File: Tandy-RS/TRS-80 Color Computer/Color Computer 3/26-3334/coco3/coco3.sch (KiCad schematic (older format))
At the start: 5 parts, among them CN1 Conn_02x20_Odd_Even

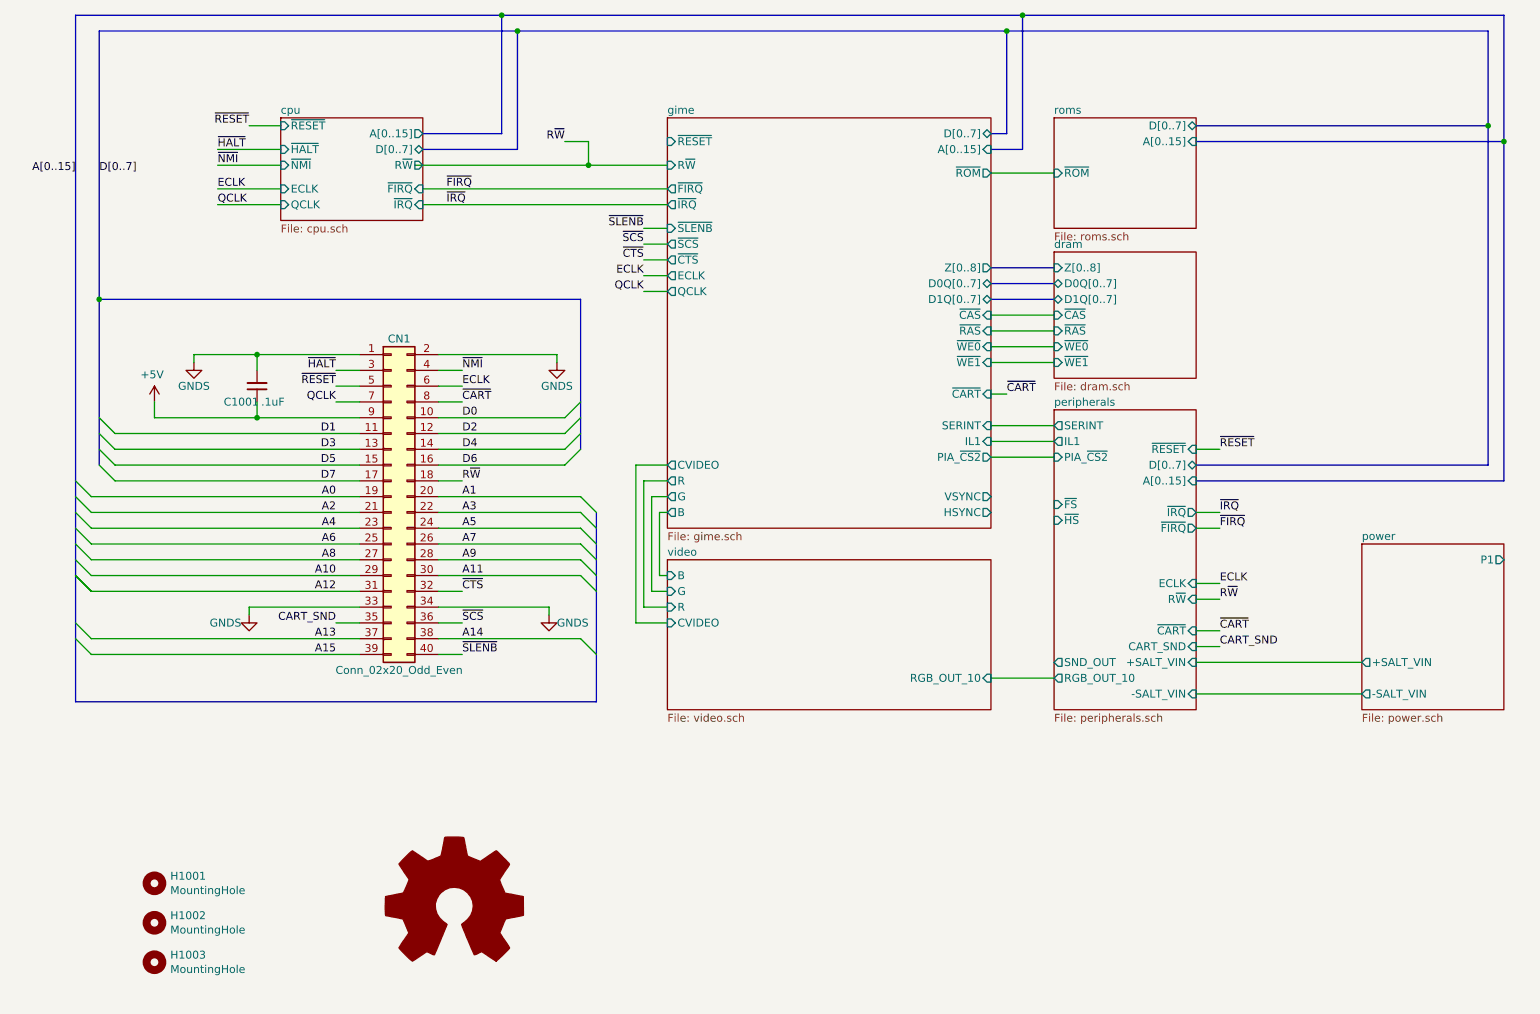
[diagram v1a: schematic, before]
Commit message: cleaned up the peripherals sheet a little
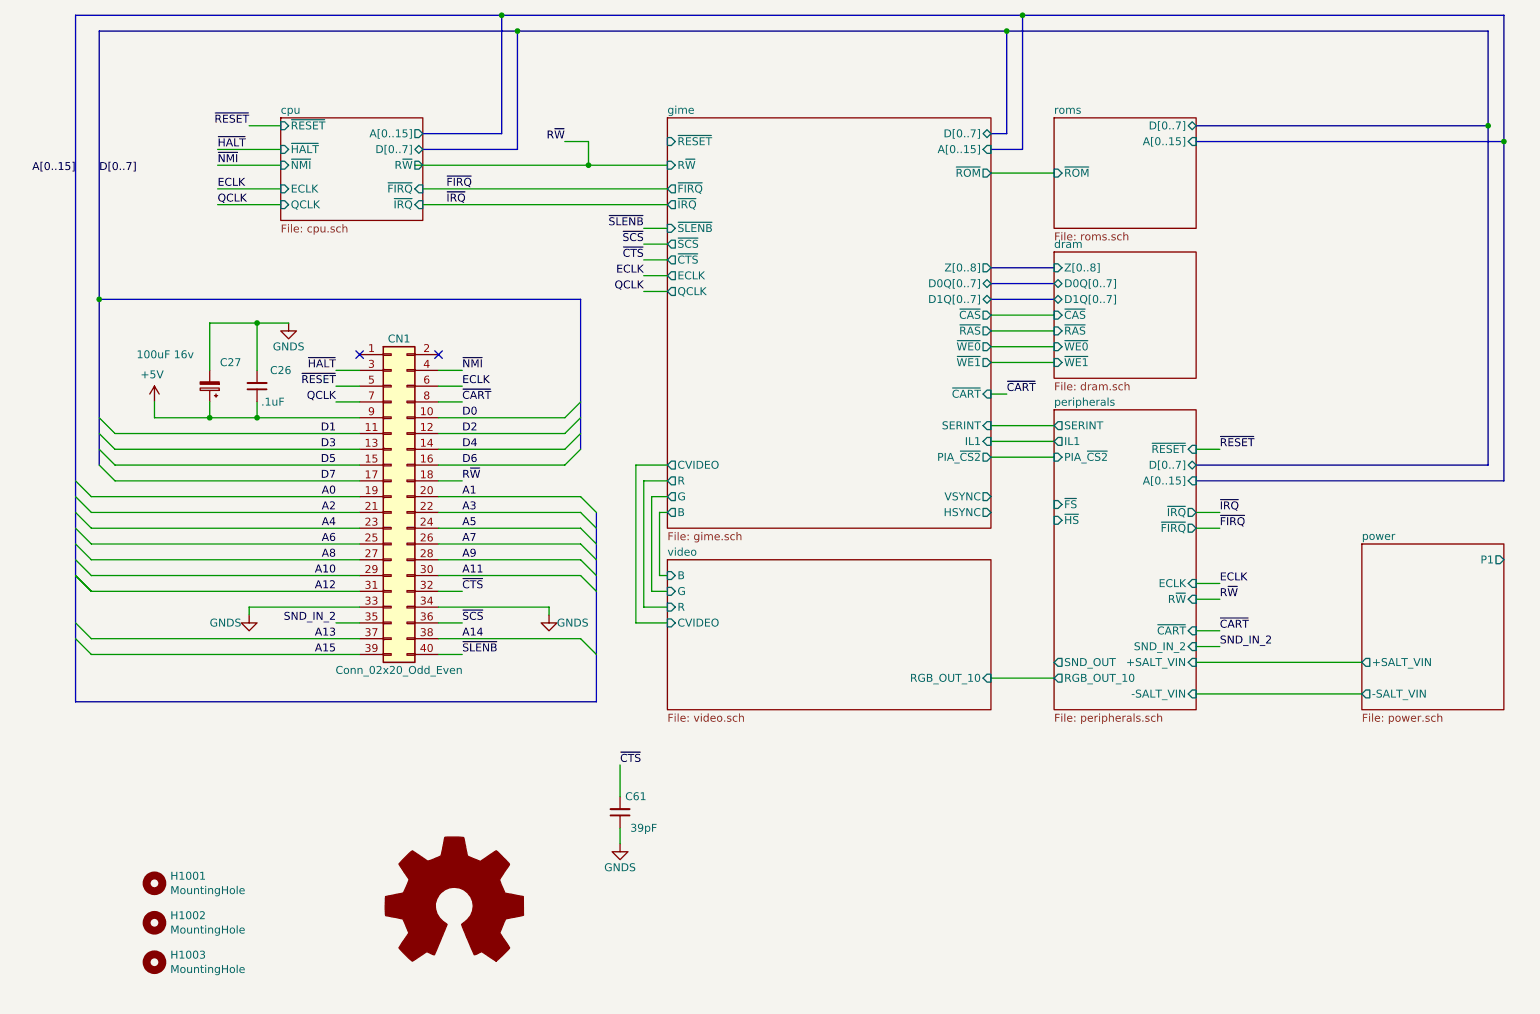
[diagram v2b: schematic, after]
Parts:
- added C27: 100uF 16v, Capacitor_THT:CP_Radial_D8.0mm_P5.00mm, symbol Device:CP_Small
- added C61: 39pF, Capacitor_THT:C_Disc_D4.7mm_W2.5mm_P5.00mm, symbol Device:C_Small
- renumbered C1001 to C26
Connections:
- net +5V: now also C27.1
- net GNDS: now also C27.2, C61.1; no longer CN1.1 (Pin_1), CN1.2 (Pin_2)
- net ~CTS: now also C61.2
- net CART_SND renamed SND_IN_2
- no-connect marks 0 -> 2
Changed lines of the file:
@@
 	8100 5350 7950 5350
 Text Label 8100 5450 0    50   ~ 0
-CART_SND
+SND_IN_2
 Wire Wire Line
 	8100 5450 7950 5450
@@
 D[0..7]
 Wire Wire Line
-	2000 3600 2650 3600
-Wire Wire Line
 	2000 4000 2650 4000
 Connection ~ 2000 4000
 Wire Wire Line
 	2000 3900 2000 4000
-Connection ~ 2000 3600
-Wire Wire Line
-	2000 3700 2000 3600
-Wire Wire Line
-	1600 3600 2000 3600
-Wire Wire Line
-	1350 4000 2000 4000
+Wire Wire Line
+	1350 4000 1700 4000
 Wire Wire Line
 	1100 4400 2650 4400
@@
 Text Label 3300 4400 0    50   ~ 0
 R~W
-Text Label 2500 5300 2    50   ~ 0
-CART_SND
 Text Label 3300 3900 0    50   ~ 0
 ~CART
@@
 Wire Wire Line
 	1350 4000 1350 3900
-Wire Wire Line
-	1600 3600 1600 3650
 $Comp
 L power:GNDS #PWR?
 U 1 1 60A48794
-P 1600 3650
+P 2200 3400
 AR Path="/602A51A8/60A48794" Ref="#PWR?"  Part="1"
 AR Path="/60308A73/60A48794" Ref="#PWR?"  Part="1"
@@
 AR Path="/603D345E/60A48794" Ref="#PWR?"  Part="1"
 AR Path="/60A48794" Ref="#PWR01001"  Part="1"
-F 0 "#PWR01001" H 1600 3400 50  0001 C CNN
-F 1 "GNDS" H 1600 3500 50  0000 C CNN
-F 2 "" H 1600 3650 50  0001 C CNN
-F 3 "" H 1600 3650 50  0001 C CNN
-	1    1600 3650
-	1    0    0    -1
-$EndComp
-Wire Wire Line
-	3150 3600 3900 3600
-Wire Wire Line
-	3900 3650 3900 3600
-$Comp
-L power:GNDS #PWR?
-U 1 1 60A3AC34
-P 3900 3650
-AR Path="/602A51A8/60A3AC34" Ref="#PWR?"  Part="1"
-AR Path="/60308A73/60A3AC34" Ref="#PWR?"  Part="1"
-AR Path="/603E4732/60A3AC34" Ref="#PWR?"  Part="1"
-AR Path="/603D345E/60A3AC34" Ref="#PWR?"  Part="1"
-AR Path="/60A3AC34" Ref="#PWR01002"  Part="1"
-F 0 "#PWR01002" H 3900 3400 50  0001 C CNN
-F 1 "GNDS" H 3900 3500 50  0000 C CNN
-F 2 "" H 3900 3650 50  0001 C CNN
-F 3 "" H 3900 3650 50  0001 C CNN
-	1    3900 3650
-	-1   0    0    -1
+F 0 "#PWR01001" H 2200 3150 50  0001 C CNN
+F 1 "GNDS" H 2200 3250 50  0000 C CNN
+F 2 "" H 2200 3400 50  0001 C CNN
+F 3 "" H 2200 3400 50  0001 C CNN
+	1    2200 3400
+	1    0    0    -1
 $EndComp
 Wire Wire Line
@@
 P 2000 3800
 AR Path="/60273794/6093C001" Ref="C?"  Part="1"
-AR Path="/6093C001" Ref="C1001"  Part="1"
-F 0 "C1001" H 2100 3900 50  0000 C CNN
+AR Path="/6093C001" Ref="C26"  Part="1"
+F 0 "C26" H 1850 3700 50  0000 C CNN
 F 1 ".1uF" H 1900 3900 50  0000 C CNN
 F 2 "Capacitor_THT:C_Disc_D4.7mm_W2.5mm_P5.00mm" H 2000 3800 50  0001 C CNN
@@
 F10 "~CART" I R 7950 5350 50
 F11 "SND_OUT" O L 7050 5550 50
-F12 "CART_SND" I R 7950 5450 50
-F13 "~FIRQ" O R 7950 4700 50
-F14 "~FS" I L 7050 4550 50
-F15 "SERINT" O L 7050 4050 50
-F16 "RGB_OUT_10" O L 7050 5650 50
-F17 "PIA_~CS2" I L 7050 4250 50
-F18 "ECLK" I R 7950 5050 50
-F19 "IL1" O L 7050 4150 50
-$EndSheet
-$Sheet
-S 4600 2100 2050 2600
-U 61257512
-F0 "gime" 50
-F1 "gime.sch" 50
-F2 "~IRQ" O L 4600 2650 50
-F3 "~FIRQ" O L 4600 2550 50
-F4 "~WE0" I R 6650 3550 50
-F5 "~WE1" I R 6650 3650 50
-F6 "~RESET" I L 4600 2250 50
-F7 "R~W" I L 4600 2400 50
-F8 "~CAS" I R 6650 3350 50
-F9 "~RAS" I R 6650 3450 50
-F10 "D0Q[0..7]" B R 6650 3150 50
-F11 "D1Q[0..7]" B R 6650 3250 50
-F12 "Z[0..8]" O R 6650 3050 50
-F13 "D[0..7]" B R 6650 2200 50
-F14 "A[0..15]" I R 6650 2300 50
-F15 "R" O L 4600 4400 50
-F16 "G" O L 4600 4500 50
-F17 "B" O L 4600 4600 50
-F18 "CVIDEO" O L 4600 4300 50
-F19 "SERINT" I R 6650 4050 50
-F20 "IL1" I R 6650 4150 50
-F21 "~CART" I R 6650 3850 50
-F22 "~SLENB" I L 4600 2800 50
-F23 "~SCS" O L 4600 2900 50
-F24 "~CTS" O L 4600 3000 50
-F25 "~ROM" O R 6650 2450 50
-F26 "PIA_~CS2" O R 6650 4250 50
-F27 "ECLK" O L 4600 3100 50
-F28 "QCLK" O L 4600 3200 50
-F29 "VSYNC" O R 6650 4500 50
-F30 "HSYNC" O R 6650 4600 50
+F12 "~FIRQ" O R 7950 4700 50
+F13 "~FS" I L 7050 4550 50
+F14 "SERINT" O L 7050 4050 50
+F15 "RGB_OUT_10" O L 7050 5650 50
+F16 "PIA_~CS2" I L 7050 4250 50
+F17 "ECLK" I R 7950 5050 50
+F18 "IL1" O L 7050 4150 50
+F19 "SND_IN_2" I R 7950 5450 50
 $EndSheet
 Wire Bus Line
@@
 Wire Wire Line
 	4600 3200 4450 3200
+$Sheet
+S 4600 2100 2050 2600
+U 61257512
+F0 "gime" 50
+F1 "gime.sch" 50
+F2 "~IRQ" O L 4600 2650 50
+F3 "~FIRQ" O L 4600 2550 50
+F4 "~RESET" I L 4600 2250 50
+F5 "R~W" I L 4600 2400 50
+F6 "D0Q[0..7]" B R 6650 3150 50
+F7 "D1Q[0..7]" B R 6650 3250 50
+F8 "Z[0..8]" O R 6650 3050 50
+F9 "D[0..7]" B R 6650 2200 50
+F10 "A[0..15]" I R 6650 2300 50
+F11 "R" O L 4600 4400 50
+F12 "G" O L 4600 4500 50
+F13 "B" O L 4600 4600 50
+F14 "CVIDEO" O L 4600 4300 50
+F15 "SERINT" I R 6650 4050 50
+F16 "IL1" I R 6650 4150 50
+F17 "~CART" I R 6650 3850 50
+F18 "~SLENB" I L 4600 2800 50
+F19 "~SCS" O L 4600 2900 50
+F20 "~CTS" O L 4600 3000 50
+F21 "~ROM" O R 6650 2450 50
+F22 "PIA_~CS2" O R 6650 4250 50
+F23 "ECLK" O L 4600 3100 50
+F24 "QCLK" O L 4600 3200 50
+F25 "VSYNC" O R 6650 4500 50
+F26 "HSYNC" O R 6650 4600 50
+F27 "~WE0" O R 6650 3550 50
+F28 "~WE1" O R 6650 3650 50
+F29 "~CAS" O R 6650 3350 50
+F30 "~RAS" O R 6650 3450 50
+$EndSheet
+NoConn ~ 2650 3600
+NoConn ~ 3150 3600
+$Comp
+L Device:CP_Small C?
+U 1 1 613747DC
+P 1700 3800
+AR Path="/602A51A8/613747DC" Ref="C?"  Part="1"
+AR Path="/603CF7B8/613747DC" Ref="C?"  Part="1"
+AR Path="/613747DC" Ref="C27"  Part="1"
+F 0 "C27" H 1500 3650 50  0000 L CNN
+F 1 "100uF 16v" H 1800 3600 50  0000 L CNN
+F 2 "Capacitor_THT:CP_Radial_D8.0mm_P5.00mm" H 1700 3800 50  0001 C CNN
+F 3 "http://nichicon-us.com/english/products/pdfs/e-uvz.pdf" H 1700 3800 50  0001 C CNN
+F 4 "digikey" H 1700 3800 50  0001 C CNN "Vendor"
+F 5 "493-17434-1-ND" H 1700 3800 50  0001 C CNN "Vendor part#"
+F 6 "UST1C101MDD1TA" H 1700 3800 50  0001 C CNN "Manufacturer part#"
+	1    1700 3800
+	-1   0    0    1
+$EndComp
+Wire Wire Line
+	1700 3900 1700 4000
+Connection ~ 1700 4000
+Wire Wire Line
+	1700 4000 2000 4000
+Wire Wire Line
+	2200 3400 2000 3400
+Wire Wire Line
+	1700 3400 1700 3700
+Wire Wire Line
+	2000 3400 2000 3700
+Connection ~ 2000 3400
+Wire Wire Line
+	2000 3400 1700 3400
+$Comp
+L Device:C_Small C?
+U 1 1 613A25D3
+P 4300 6500
+AR Path="/60273794/613A25D3" Ref="C?"  Part="1"
+AR Path="/602A51A8/613A25D3" Ref="C?"  Part="1"
+AR Path="/603CF7B8/613A25D3" Ref="C?"  Part="1"
+AR Path="/61257512/613A25D3" Ref="C?"  Part="1"
+AR Path="/613A25D3" Ref="C61"  Part="1"
+F 0 "C61" H 4400 6400 50  0000 C CNN
+F 1 "39pF" H 4450 6600 50  0000 C CNN
+F 2 "Capacitor_THT:C_Disc_D4.7mm_W2.5mm_P5.00mm" H 4300 6500 50  0001 C CNN
+F 3 " https://www.vishay.com/docs/45171/kseries.pdf" H 4300 6500 50  0001 C CNN
+F 4 "digikey" V 4300 6500 50  0001 C CNN "Vendor"
+F 5 "BC1008CT-ND" V 4300 6500 50  0001 C CNN "Vendor part#"
+F 6 "K390J15C0GF5TL2" V 4300 6500 50  0001 C CNN "Manufacturer part#"
+	1    4300 6500
+	1    0    0    1
+$EndComp
+$Comp
+L power:GNDS #PWR?
+U 1 1 613BBC94
+P 4300 6700
+AR Path="/602A51A8/613BBC94" Ref="#PWR?"  Part="1"
+AR Path="/60308A73/613BBC94" Ref="#PWR?"  Part="1"
+AR Path="/603E4732/613BBC94" Ref="#PWR?"  Part="1"
+AR Path="/603D345E/613BBC94" Ref="#PWR?"  Part="1"
+AR Path="/613BBC94" Ref="#PWR01002"  Part="1"
+F 0 "#PWR01002" H 4300 6450 50  0001 C CNN
+F 1 "GNDS" H 4300 6550 50  0000 C CNN
+F 2 "" H 4300 6700 50  0001 C CNN
+F 3 "" H 4300 6700 50  0001 C CNN
+	1    4300 6700
+	1    0    0    -1
+$EndComp
+Text Label 4300 6200 0    50   ~ 0
+~CTS
+Wire Wire Line
+	4300 6200 4300 6400
+Wire Wire Line
+	4300 6600 4300 6700
 Wire Bus Line
 	1000 3250 1000 4300
@@
 Wire Bus Line
 	850  1450 850  5800
+Text Label 2500 5300 2    50   ~ 0
+SND_IN_2
 $EndSCHEMATC

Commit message: finished peripherals sheet
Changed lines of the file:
@@
 F7 "~RESET" I R 7950 4200 50
 F8 "A[0..15]" I R 7950 4400 50
-F9 "~HS" I L 7050 4650 50
-F10 "~CART" I R 7950 5350 50
-F11 "SND_OUT" O L 7050 5550 50
-F12 "~FIRQ" O R 7950 4700 50
-F13 "~FS" I L 7050 4550 50
-F14 "SERINT" O L 7050 4050 50
-F15 "RGB_OUT_10" O L 7050 5650 50
-F16 "PIA_~CS2" I L 7050 4250 50
-F17 "ECLK" I R 7950 5050 50
-F18 "IL1" O L 7050 4150 50
-F19 "SND_IN_2" I R 7950 5450 50
+F9 "~CART" I R 7950 5350 50
+F10 "SND_OUT" O L 7050 5550 50
+F11 "~FIRQ" O R 7950 4700 50
+F12 "SERINT" O L 7050 4050 50
+F13 "RGB_OUT_10" O L 7050 5650 50
+F14 "PIA_~CS2" I L 7050 4250 50
+F15 "ECLK" I R 7950 5050 50
+F16 "IL1" O L 7050 4150 50
+F17 "SND_IN_2" I R 7950 5450 50
+F18 "~VSYNC" I L 7050 4350 50
+F19 "~HSYNC" I L 7050 4450 50
 $EndSheet
 Wire Bus Line
@@
 F23 "ECLK" O L 4600 3100 50
 F24 "QCLK" O L 4600 3200 50
-F25 "VSYNC" O R 6650 4500 50
-F26 "HSYNC" O R 6650 4600 50
+F25 "VSYNC" O L 4600 4100 50
+F26 "HSYNC" O L 4600 4200 50
 F27 "~WE0" O R 6650 3550 50
 F28 "~WE1" O R 6650 3650 50
 F29 "~CAS" O R 6650 3350 50
 F30 "~RAS" O R 6650 3450 50
+F31 "~VSYNC" O R 6650 4350 50
+F32 "~HSYNC" O R 6650 4450 50
 $EndSheet
 NoConn ~ 2650 3600
@@
 Wire Wire Line
 	4300 6600 4300 6700
-Wire Bus Line
-	1000 3250 1000 4300
-Wire Bus Line
-	4050 3250 4050 4200
-Wire Bus Line
-	4150 4600 4150 5800
-Wire Bus Line
-	850  1450 850  5800
 Text Label 2500 5300 2    50   ~ 0
 SND_IN_2
+Wire Wire Line
+	6650 4350 7050 4350
+Wire Wire Line
+	7050 4450 6650 4450
+Wire Bus Line
+	1000 3250 1000 4300
+Wire Bus Line
+	4050 3250 4050 4200
+Wire Bus Line
+	4150 4600 4150 5800
+Wire Bus Line
+	850  1450 850  5800
 $EndSCHEMATC

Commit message: added more stuff to the video sheet
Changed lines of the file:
@@
 F5 "G" I L 4600 5100 50
 F6 "B" I L 4600 5000 50
+F7 "HSYNC" I L 4600 5400 50
+F8 "VSYNC" I L 4600 5500 50
 $EndSheet
 Wire Wire Line
@@
 Wire Wire Line
 	7050 4450 6650 4450
+Wire Wire Line
+	4600 4200 4350 4200
+Wire Wire Line
+	4350 4200 4350 5400
+Wire Wire Line
+	4350 5400 4600 5400
+Wire Wire Line
+	4600 4100 4300 4100
+Wire Wire Line
+	4300 4100 4300 5500
+Wire Wire Line
+	4300 5500 4600 5500
 Wire Bus Line
 	1000 3250 1000 4300

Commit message: added some more to the video sheet
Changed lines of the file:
@@
 F8 "A[0..15]" I R 7950 4400 50
 F9 "~CART" I R 7950 5350 50
-F10 "SND_OUT" O L 7050 5550 50
-F11 "~FIRQ" O R 7950 4700 50
-F12 "SERINT" O L 7050 4050 50
-F13 "RGB_OUT_10" O L 7050 5650 50
-F14 "PIA_~CS2" I L 7050 4250 50
-F15 "ECLK" I R 7950 5050 50
-F16 "IL1" O L 7050 4150 50
-F17 "SND_IN_2" I R 7950 5450 50
-F18 "~VSYNC" I L 7050 4350 50
-F19 "~HSYNC" I L 7050 4450 50
+F10 "~FIRQ" O R 7950 4700 50
+F11 "SERINT" O L 7050 4050 50
+F12 "RGB_OUT_10" O L 7050 5650 50
+F13 "PIA_~CS2" I L 7050 4250 50
+F14 "ECLK" I R 7950 5050 50
+F15 "IL1" O L 7050 4150 50
+F16 "SND_IN_2" I R 7950 5450 50
+F17 "~VSYNC" I L 7050 4350 50
+F18 "~HSYNC" I L 7050 4450 50
+F19 "SOUND" O L 7050 5550 50
 $EndSheet
 Wire Bus Line
@@
 F7 "HSYNC" I L 4600 5400 50
 F8 "VSYNC" I L 4600 5500 50
+F9 "SOUND" I R 6650 5550 50
 $EndSheet
 Wire Wire Line
@@
 Wire Wire Line
 	4300 5500 4600 5500
+Wire Wire Line
+	7050 5550 6650 5550
 Wire Bus Line
 	1000 3250 1000 4300
